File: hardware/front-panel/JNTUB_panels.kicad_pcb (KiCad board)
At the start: 2 copper layers, 128 x 128.5 mm, 18 parts

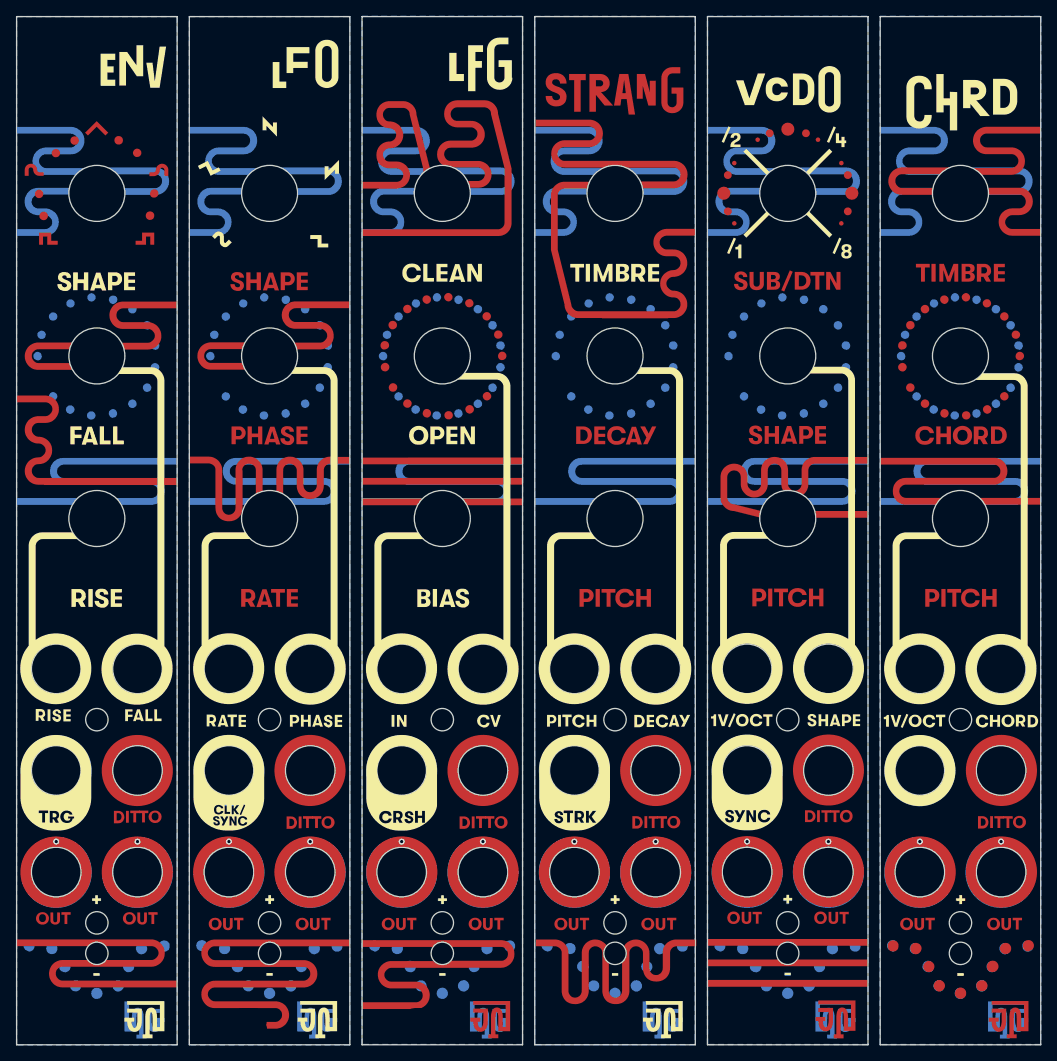
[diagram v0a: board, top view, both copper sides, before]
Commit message: [JNTUB-HW] Prepare a smaller mfg batch of panels
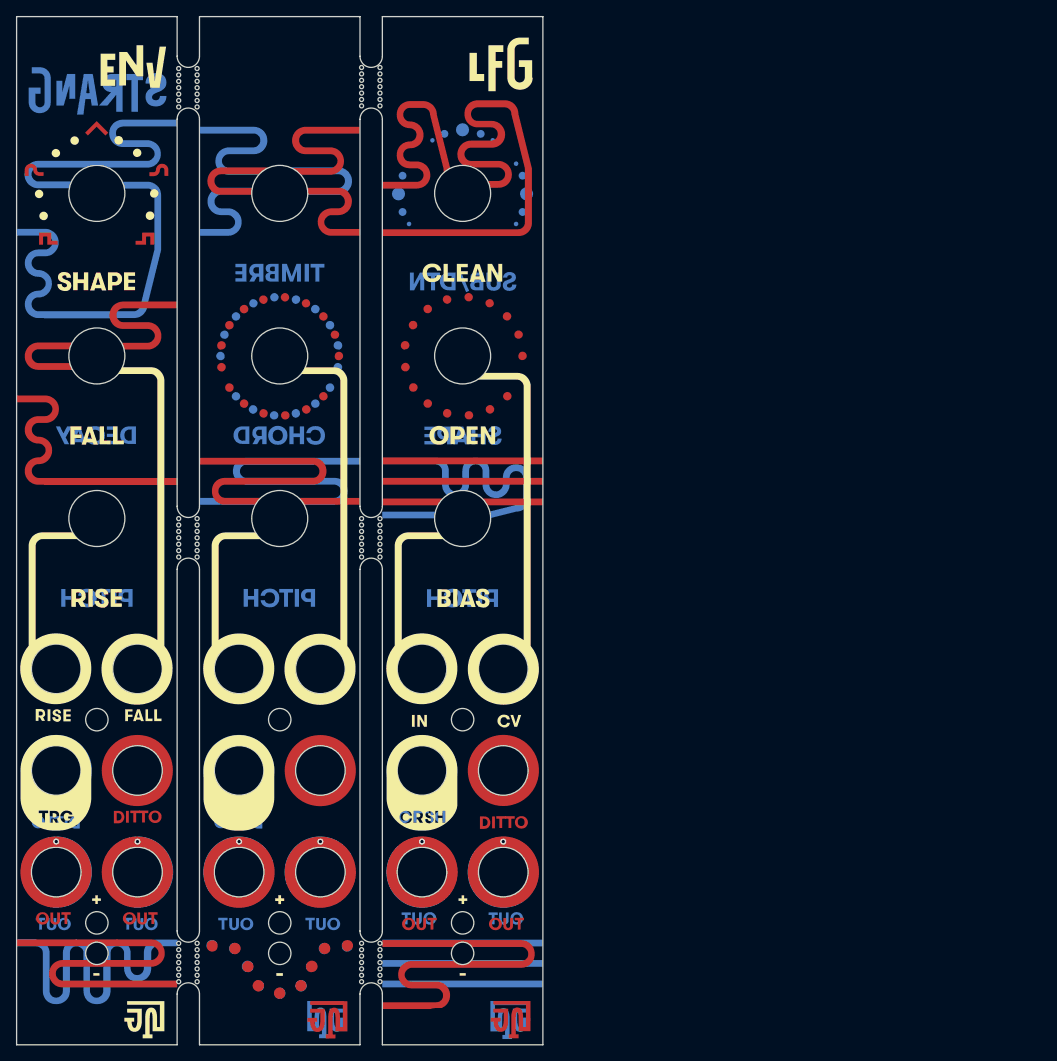
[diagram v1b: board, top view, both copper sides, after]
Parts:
- removed the REF** at (179.1, 86.4)
- removed the REF** at (157.5, 86.4)
- removed the REF** at (200.7, 86.4)
- removed the svg2mod at (92.7, 94.4)
- removed the svg2mod at (114.3, 94.4)
- removed the svg2mod at (135.9, 94.4)
- removed the svg2mod at (157.5, 94.4)
- removed the svg2mod at (179.1, 94.4)
- removed the svg2mod at (200.6, 94.4)
- removed the svg2mod at (114.3, 88.9)
- added mouse-bite-2.8mm-slot: VAL**, Panelization:mouse-bite-2.8mm-slot-long, F.Cu at (127.0, 141.9)
- added mouse-bite-2.8mm-slot: VAL**, Panelization:mouse-bite-2.8mm-slot-long, F.Cu at (127.0, 88.8)
- added mouse-bite-2.8mm-slot: VAL**, Panelization:mouse-bite-2.8mm-slot-long, F.Cu at (127.0, 32.4)
- added mouse-bite-2.8mm-slot: VAL**, Panelization:mouse-bite-2.8mm-slot-long, F.Cu at (104.1, 141.9)
- added mouse-bite-2.8mm-slot: VAL**, Panelization:mouse-bite-2.8mm-slot-long, F.Cu at (104.1, 88.8)
- added mouse-bite-2.8mm-slot: VAL**, Panelization:mouse-bite-2.8mm-slot-long, F.Cu at (104.1, 32.5)
- added svg2mod: G***, Panels:plain, F.Cu at (115.6, 94.4)
- svg2mod (x3): moved to B.Cu
- moved svg2mod 85.1 mm to (115.6, 91.1), turned to 180 degrees
- moved svg2mod 64.9 mm to (92.7, 90.6), turned to 180 degrees
- moved svg2mod 40.7 mm to (138.4, 90.7), turned to 180 degrees
- moved REF** 2.54 mm to (138.4, 86.4)
- moved svg2mod 2.54 mm to (138.4, 88.8)
- moved REF** 1.27 mm to (115.6, 86.4)
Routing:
- net (no net): vias 12 -> 6
- removed copper zone on B.Cu, net (none)
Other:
- board size 128 x 128.5 mm -> 65.8 x 128.5 mm
